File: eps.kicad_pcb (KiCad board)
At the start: 4 copper layers, 90 x 96 mm, 43 parts, among them J1 Barrel_Jack, U1 LT3652EMSE

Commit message: Solved errors
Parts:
- moved J1 12.0 mm to (118.7, 106.0)
- moved D9 3.71 mm to (169.0, 36.0)
- moved REF** 1.72 mm to (103.0, 126.0)
- moved REF** 1.47 mm to (103.0, 36.0)
- moved REF** 1.39 mm to (187.0, 126.0)
- moved D10 1.33 mm to (161.3, 36.1)
- moved REF** 1.06 mm to (187.0, 36.0)
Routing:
- net Net-(U1-SENSE): track 33.5 -> 19.9 mm
- net GND: track 275.2 -> 286.4 mm
- net Net-(D7-A): track 56.3 -> 61.5 mm
- net /BatteryCharger/in: track 100.4 -> 96.9 mm
- net Net-(D9-K): track 9.61 -> 8.70 mm
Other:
- outline, holes or cut-outs redrawn
- board text added: "Hydrogen v0.1"
- board text added: "Ulog3"

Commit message: final
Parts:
- added J2: Conn_01x02_Pin, Connector_PinHeader_2.00mm:PinHeader_1x02_P2.00mm_Vertical, B.Cu at (126.0, 34.0)
- SC1, SC2, SC3, SC4, SC5, SC6: footprint Connector_PinHeader_1.00mm:PinHeader_2x01_P1.00mm_Vertical -> Connector_PinHeader_2.00mm:PinHeader_1x02_P2.00mm_Vertical
- moved D9 7.51 mm to (176.3, 34.0)
- moved SC6 7.27 mm to (162.0, 34.0), turned to -90 degrees
- moved D10 6.76 mm to (167.8, 34.1)
- moved SC5 5.50 mm to (156.0, 34.0), turned to -90 degrees
- moved SC4 3.79 mm to (149.9, 34.0), turned to -90 degrees
- moved SC1 2.56 mm to (131.6, 34.0), turned to -90 degrees
- moved SC3 2.25 mm to (143.8, 34.0), turned to -90 degrees
- moved SC2 1.57 mm to (137.7, 34.0), turned to -90 degrees
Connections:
- net VBUS renamed /BatteryCharger/load
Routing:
- net /BatteryCharger/load: track 33.6 -> 61.0 mm
- net Net-(U1-SENSE): track 19.9 -> 46.2 mm
- net GND: track 286.4 -> 302.3 mm
- net /BatteryCharger/in: track 96.9 -> 110.8 mm
- net Net-(D9-K): track 8.70 -> 10.7 mm
- net Net-(D2-A): track 6.74 -> 8.53 mm
- net Net-(D3-A): track 6.81 -> 8.12 mm
- net Net-(D1-A): track 6.99 -> 8.11 mm
- net Net-(D4-A): track 7.36 -> 8.33 mm
- net Net-(D5-A): track 7.91 -> 8.54 mm
- net Net-(D10-K): track 9.74 -> 9.18 mm

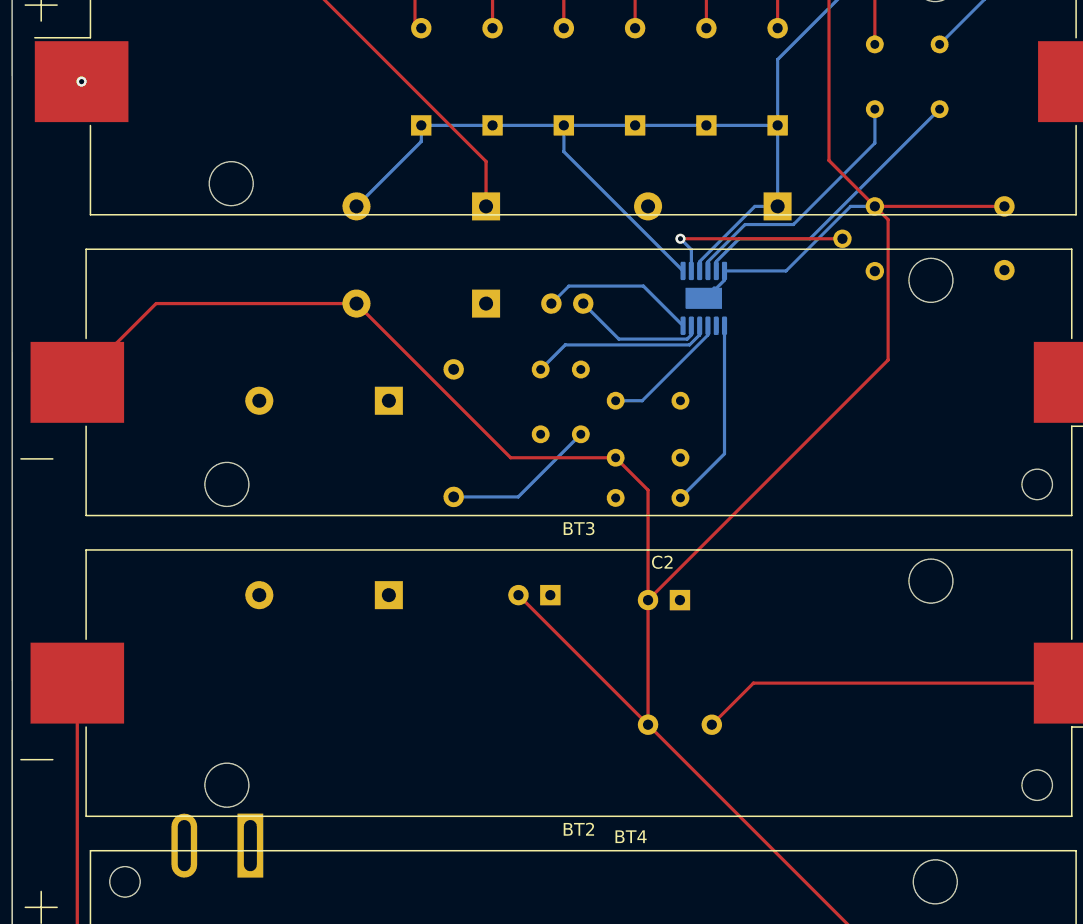
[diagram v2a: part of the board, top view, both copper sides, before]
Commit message: 2layerconversion
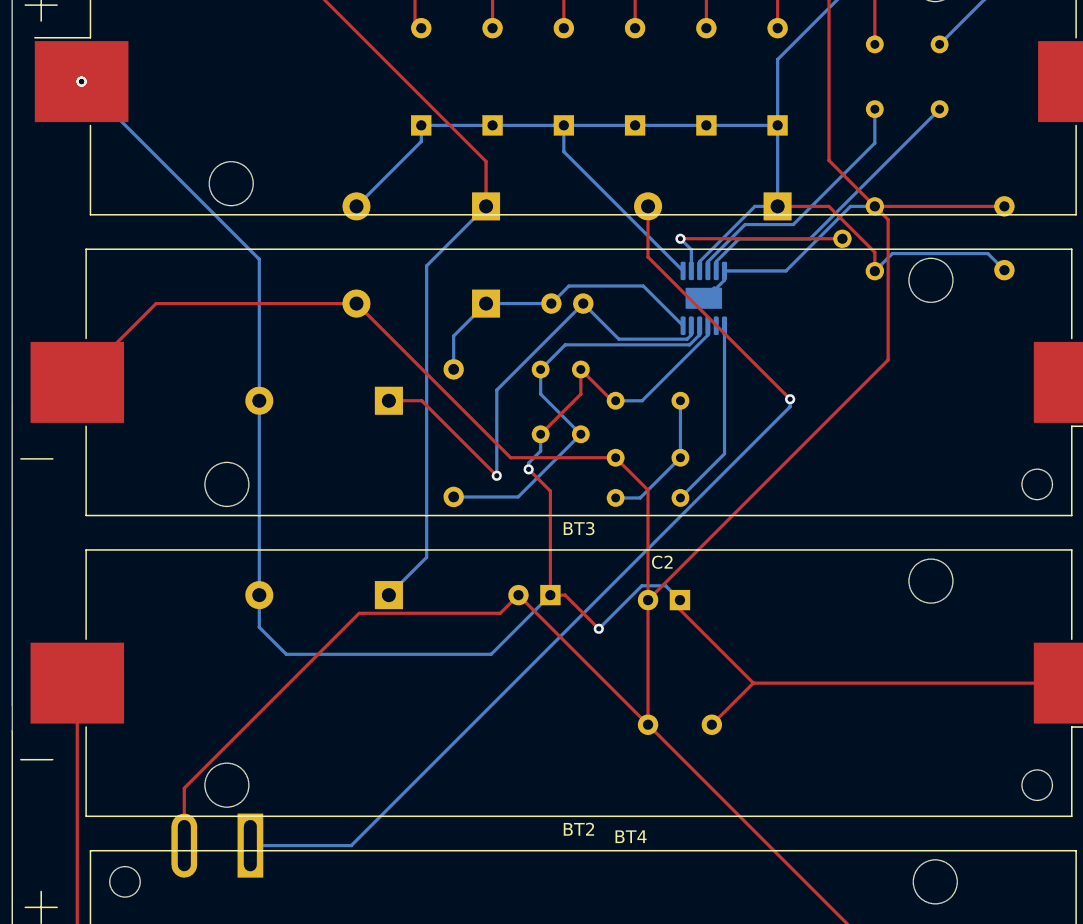
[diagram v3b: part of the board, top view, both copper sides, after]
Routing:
- net Net-(D7-A): track 61.5 -> 76.9 mm, vias 0 -> 1
- net Net-(U1-SENSE): track 46.2 -> 33.4 mm
- net Net-(D11-K): track 28.9 -> 37.7 mm, vias 0 -> 1
- net Net-(BT1-+): track 158.2 -> 163.0 mm, vias 1 -> 4
- net GND: track 302.3 -> 300.9 mm
- net /BatteryCharger/in: track 110.8 -> 111.7 mm
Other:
- copper layers 4 -> 2

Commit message: Added
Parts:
- added J3: Conn_01x02_Pin, Connector_PinHeader_2.00mm:PinHeader_1x02_P2.00mm_Vertical, B.Cu at (88.0, 43.9)
- added J4: Conn_01x02_Pin, Connector_PinHeader_2.00mm:PinHeader_1x02_P2.00mm_Vertical, B.Cu at (83.9, 43.9)
- added J5: Conn_01x02_Pin, Connector_PinHeader_2.00mm:PinHeader_1x02_P2.00mm_Vertical, B.Cu at (79.9, 43.9)
- added J6: Conn_01x02_Pin, Connector_PinHeader_2.00mm:PinHeader_1x02_P2.00mm_Vertical, B.Cu at (75.8, 43.9)
- added R8: R, Resistor_THT:R_Axial_DIN0204_L3.6mm_D1.6mm_P5.08mm_Horizontal, B.Cu at (88.5, 51.5)
- added R9: R, Resistor_THT:R_Axial_DIN0204_L3.6mm_D1.6mm_P5.08mm_Horizontal, B.Cu at (78.5, 51.5)
- added U2: INA234AxYBJ, Package_BGA:Texas_DSBGA-8_0.705x1.468mm_Layout2x4_P0.4mm, B.Cu at (88.1, 55.3)
- added U3: INA234AxYBJ, Package_BGA:Texas_DSBGA-8_0.705x1.468mm_Layout2x4_P0.4mm, B.Cu at (78.1, 55.3)
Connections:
- net /BatteryCharger/load renamed +5V
- D1 pad 1: /BatteryCharger/in -> /Power sensor/source
- D13 pad 2: Net-(BT1-+) -> Net-(D13-A)
- D2 pad 1: /BatteryCharger/in -> /Power sensor/source
- D3 pad 1: /BatteryCharger/in -> /Power sensor/source
- D4 pad 1: /BatteryCharger/in -> /Power sensor/source
- D5 pad 1: /BatteryCharger/in -> /Power sensor/source
- D6 pad 1: /BatteryCharger/in -> /Power sensor/source

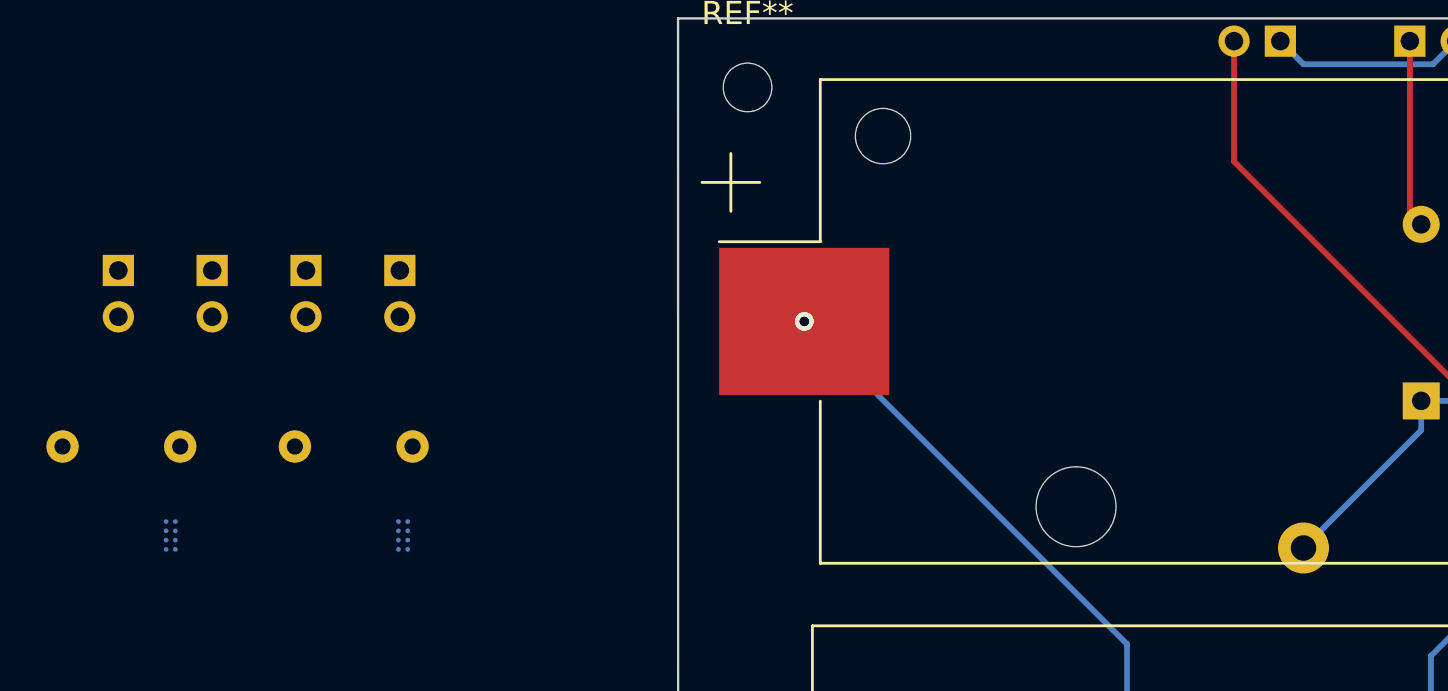
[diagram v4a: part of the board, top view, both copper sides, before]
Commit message: changed placement
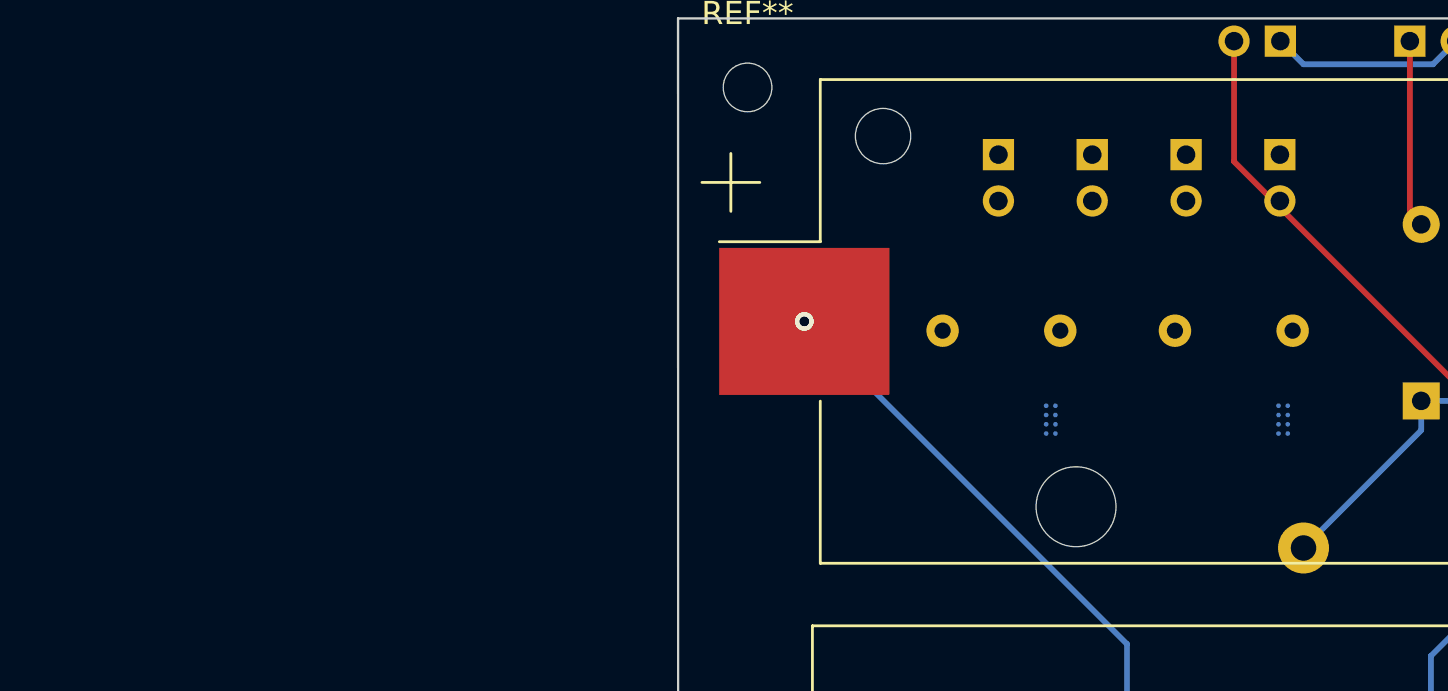
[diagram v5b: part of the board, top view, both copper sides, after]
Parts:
- moved J3 38.3 mm to (126.0, 38.9)
- moved J4 38.3 mm to (121.9, 38.9)
- moved U2 38.3 mm to (126.1, 50.3)
- moved U3 38.3 mm to (116.1, 50.3)
- moved J5 38.3 mm to (117.9, 38.9)
- moved J6 38.3 mm to (113.8, 38.9)
- moved R8 38.3 mm to (126.5, 46.5)
- moved R9 38.3 mm to (116.5, 46.5)
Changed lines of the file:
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@@
 	(footprint "Package_BGA:Texas_DSBGA-8_0.705x1.468mm_Layout2x4_P0.4mm"
 		(layer "B.Cu")
-		(at 88.13 55.34 180)
+		(at 126.12 50.34 180)
 		(descr "Texas Instruments, DSBGA, area grid, NSMD, YBJ0008 pad definition, 0.705x1.468mm, 8 Ball, 2x4 Layout, 0.4mm Pitch, https://www.ti.com/lit/gpn/ina234")
 		(tags "BGA 8 0.4")
@@
 	(footprint "Connector_PinHeader_2.00mm:PinHeader_1x02_P2.00mm_Vertical"
 		(layer "B.Cu")
-		(at 83.94 43.9 180)
+		(at 121.93 38.9 180)
 		(descr "Through hole straight pin header, 1x02, 2.00mm pitch, single row")
 		(tags "Through hole pin header THT 1x02 2.00mm single row")
@@
 	(footprint "Connector_PinHeader_2.00mm:PinHeader_1x02_P2.00mm_Vertical"
 		(layer "B.Cu")
-		(at 75.84 43.9 180)
+		(at 113.83 38.9 180)
 		(descr "Through hole straight pin header, 1x02, 2.00mm pitch, single row")
 		(tags "Through hole pin header THT 1x02 2.00mm single row")
@@
 	(footprint "Resistor_THT:R_Axial_DIN0204_L3.6mm_D1.6mm_P5.08mm_Horizontal"
 		(layer "B.Cu")
-		(at 78.51 51.5 180)
+		(at 116.5 46.5 180)
 		(descr "Resistor, Axial_DIN0204 series, Axial, Horizontal, pin pitch=5.08mm, 0.167W, length*diameter=3.6*1.6mm^2, http://cdn-reichelt.de/documents/datenblatt/B400/1_4W%23YAG.pdf")
 		(tags "Resistor Axial_DIN0204 series Axial Horizontal pin pitch 5.08mm 0.167W length 3.6mm diameter 1.6mm")
@@
 	(footprint "Connector_PinHeader_2.00mm:PinHeader_1x02_P2.00mm_Vertical"
 		(layer "B.Cu")
-		(at 87.99 43.9 180)
+		(at 125.98 38.9 180)
 		(descr "Through hole straight pin header, 1x02, 2.00mm pitch, single row")
 		(tags "Through hole pin header THT 1x02 2.00mm single row")
@@
 	(footprint "Resistor_THT:R_Axial_DIN0204_L3.6mm_D1.6mm_P5.08mm_Horizontal"
 		(layer "B.Cu")
-		(at 88.54 51.5 180)
+		(at 126.53 46.5 180)
 		(descr "Resistor, Axial_DIN0204 series, Axial, Horizontal, pin pitch=5.08mm, 0.167W, length*diameter=3.6*1.6mm^2, http://cdn-reichelt.de/documents/datenblatt/B400/1_4W%23YAG.pdf")
 		(tags "Resistor Axial_DIN0204 series Axial Horizontal pin pitch 5.08mm 0.167W length 3.6mm diameter 1.6mm")
@@
 	(footprint "Package_BGA:Texas_DSBGA-8_0.705x1.468mm_Layout2x4_P0.4mm"
 		(layer "B.Cu")
-		(at 78.1 55.34 180)
+		(at 116.09 50.34 180)
 		(descr "Texas Instruments, DSBGA, area grid, NSMD, YBJ0008 pad definition, 0.705x1.468mm, 8 Ball, 2x4 Layout, 0.4mm Pitch, https://www.ti.com/lit/gpn/ina234")
 		(tags "BGA 8 0.4")
@@
 	(footprint "Connector_PinHeader_2.00mm:PinHeader_1x02_P2.00mm_Vertical"
 		(layer "B.Cu")
-		(at 79.89 43.9 180)
+		(at 117.88 38.9 180)
 		(descr "Through hole straight pin header, 1x02, 2.00mm pitch, single row")
 		(tags "Through hole pin header THT 1x02 2.00mm single row")

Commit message: new design
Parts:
- removed BT3, BT4: Battery_Cell, Battery:BatteryHolder_Keystone_1042_1x18650
- removed D11, D12, D13: 1N5819, Diode_THT:D_DO-41_SOD81_P10.16mm_Horizontal
- removed J1: Barrel_Jack, Connector_BarrelJack:BarrelJack_SwitchcraftConxall_RAPC10U_Horizontal
- removed J4, J5, J6: Conn_01x02_Pin, Connector_PinHeader_2.00mm:PinHeader_1x02_P2.00mm_Vertical
- removed the REF** at (103.0, 126.0)
- removed the REF** at (187.0, 126.0)
- removed the REF** at (187.0, 36.0)
- removed the REF** at (103.0, 36.0)
- removed RV1: 10k, Potentiometer_THT:Potentiometer_Bourns_3386P_Vertical
- added C10: 10uF 16V, Capacitor_SMD:C_0805_2012Metric_Pad1.18x1.45mm_HandSolder, F.Cu at (95.9, 148.6)
- added C11: 1uF, Capacitor_SMD:C_0603_1608Metric_Pad1.08x0.95mm_HandSolder, F.Cu at (97.9, 148.6)
- added C6: 0.1uF 10V, Capacitor_SMD:C_0201_0603Metric_Pad0.64x0.40mm_HandSolder, F.Cu at (136.0, 92.5)
- added C7: 10uF 10V, Capacitor_SMD:C_0805_2012Metric_Pad1.18x1.45mm_HandSolder, F.Cu at (132.0, 92.5)
- added C8: 1uF 50V, Capacitor_SMD:C_0402_1005Metric_Pad0.74x0.62mm_HandSolder, F.Cu at (113.9, 154.0)
- added C9: 100uF 10V, Capacitor_THT:C_Radial_D5.0mm_H11.0mm_P2.00mm, F.Cu at (121.0, 149.0)
- added L2: 10uH, Inductor_SMD:L_2512_6332Metric_Pad1.52x3.35mm_HandSolder, F.Cu at (121.5, 156.0)
- added R10: 100k, Resistor_THT:R_Axial_DIN0207_L6.3mm_D2.5mm_P15.24mm_Horizontal, F.Cu at (91.6, 87.3)
- added R11: 0.068, Resistor_THT:R_Axial_DIN0207_L6.3mm_D2.5mm_P15.24mm_Horizontal, F.Cu at (115.1, 150.1)
- added R12: 430k, Resistor_THT:R_Axial_DIN0207_L6.3mm_D2.5mm_P15.24mm_Horizontal, F.Cu at (78.3, 146.6)
- added R13: 606k, Resistor_THT:R_Axial_DIN0207_L6.3mm_D2.5mm_P15.24mm_Horizontal, F.Cu at (78.3, 150.1)
- added R14: 0.1, Resistor_THT:R_Axial_DIN0207_L6.3mm_D2.5mm_P15.24mm_Horizontal, F.Cu at (115.1, 146.6)
- added REF**: MountingHole_5mm, MountingHole:MountingHole_5mm, F.Cu at (132.0, 152.0)
- added REF**: MountingHole_5mm, MountingHole:MountingHole_5mm, F.Cu at (58.0, 152.0)
- added REF**: MountingHole_5mm, MountingHole:MountingHole_5mm, F.Cu at (132.5, 72.0)
- added REF**: MountingHole_5mm, MountingHole:MountingHole_5mm, F.Cu at (57.5, 72.0)
- BT1, BT2: value Battery_Cell -> 3.7v
- C1: value 10uF -> 2.2uF; footprint Capacitor_THT:C_Disc_D5.1mm_W3.2mm_P5.00mm -> Capacitor_SMD:C_0402_1005Metric_Pad0.74x0.62mm_HandSolder; moved to F.Cu
- C2: value 100uF -> 0.1uF; footprint Capacitor_THT:CP_Radial_D6.3mm_P2.50mm -> Capacitor_SMD:C_0603_1608Metric_Pad1.08x0.95mm_HandSolder; moved to F.Cu
- C3: value 1uF -> 10nF; footprint Capacitor_THT:C_Disc_D5.0mm_W2.5mm_P2.50mm -> Capacitor_SMD:C_0805_2012Metric_Pad1.18x1.45mm_HandSolder; moved to F.Cu
- C4: value 10uF -> 100pF; footprint Capacitor_THT:C_Disc_D5.1mm_W3.2mm_P5.00mm -> Capacitor_SMD:C_0402_1005Metric_Pad0.74x0.62mm_HandSolder; moved to F.Cu
- C5: value 100uF 16v -> 470pF; footprint Capacitor_THT:CP_Radial_D6.3mm_P2.50mm -> Capacitor_SMD:C_0603_1608Metric_Pad1.08x0.95mm_HandSolder; moved to F.Cu
- D1, D2, D3, D4, D5, D6: moved to F.Cu
- D10, D9: footprint LED_THT:LED_Rectangular_W3.0mm_H2.0mm -> LED_THT:LED_D5.0mm; moved to F.Cu
- D7: value 1N5819 -> MBR340; footprint Diode_THT:D_DO-41_SOD81_P10.16mm_Horizontal -> Diode_THT:D_DO-201AD_P15.24mm_Horizontal; moved to F.Cu
- D8: value 1N5819 -> 1N5817; moved to F.Cu
- J2: value Conn_01x02_Pin -> Out-; footprint Connector_PinHeader_2.00mm:PinHeader_1x02_P2.00mm_Vertical -> Connector_PinHeader_2.54mm:PinHeader_1x02_P2.54mm_Vertical; moved to F.Cu
- J3: value Conn_01x02_Pin -> NTC_PIN; footprint Connector_PinHeader_2.00mm:PinHeader_1x02_P2.00mm_Vertical -> Connector_PinHeader_2.54mm:PinHeader_1x02_P2.54mm_Vertical; moved to F.Cu
- L1: value 68uH -> 4.7uH; footprint Inductor_THT:L_Axial_L5.0mm_D3.6mm_P10.00mm_Horizontal_Murata_BL01RN1A2A2 -> Inductor_THT:L_Radial_D8.7mm_P5.00mm_Fastron_07HCP; moved to F.Cu
- R1: value 568k -> 17.8k; footprint Resistor_THT:R_Axial_DIN0204_L3.6mm_D1.6mm_P5.08mm_Horizontal -> Resistor_THT:R_Axial_DIN0207_L6.3mm_D2.5mm_P15.24mm_Horizontal; moved to F.Cu
- R2, R3: footprint Resistor_THT:R_Axial_DIN0204_L3.6mm_D1.6mm_P5.08mm_Horizontal -> Resistor_THT:R_Axial_DIN0207_L6.3mm_D2.5mm_P15.24mm_Horizontal; moved to F.Cu
- R4: value 0.22 -> 4.32k; footprint Resistor_THT:R_Axial_DIN0204_L3.6mm_D1.6mm_P5.08mm_Horizontal -> Resistor_THT:R_Axial_DIN0207_L6.3mm_D2.5mm_P15.24mm_Horizontal; moved to F.Cu
- R5: value 0.5 -> 200k; footprint Resistor_THT:R_Axial_DIN0204_L3.6mm_D1.6mm_P5.08mm_Horizontal -> Resistor_THT:R_Axial_DIN0207_L6.3mm_D2.5mm_P15.24mm_Horizontal; moved to F.Cu
- R6: value 446k -> 23.2k; footprint Resistor_THT:R_Axial_DIN0204_L3.6mm_D1.6mm_P5.08mm_Horizontal -> Resistor_THT:R_Axial_DIN0207_L6.3mm_D2.5mm_P15.24mm_Horizontal; moved to F.Cu
- R7: value 200k -> 38.3k; footprint Resistor_THT:R_Axial_DIN0204_L3.6mm_D1.6mm_P5.08mm_Horizontal -> Resistor_THT:R_Axial_DIN0207_L6.3mm_D2.5mm_P15.24mm_Horizontal; moved to F.Cu
- R8: value R -> 100k; footprint Resistor_THT:R_Axial_DIN0204_L3.6mm_D1.6mm_P5.08mm_Horizontal -> Resistor_THT:R_Axial_DIN0207_L6.3mm_D2.5mm_P15.24mm_Horizontal; moved to F.Cu
- R9: value R -> 210k; footprint Resistor_THT:R_Axial_DIN0204_L3.6mm_D1.6mm_P5.08mm_Horizontal -> Resistor_THT:R_Axial_DIN0207_L6.3mm_D2.5mm_P15.24mm_Horizontal; moved to F.Cu
- SC1, SC2, SC3, SC4, SC5, SC6: footprint Connector_PinHeader_2.00mm:PinHeader_1x02_P2.00mm_Vertical -> Connector_PinHeader_2.54mm:PinHeader_1x02_P2.54mm_Vertical; moved to F.Cu
- U1: value LT3652EMSE -> LT3652IMSE; moved to F.Cu
- U2: value INA234AxYBJ -> CMSH3-40MA; footprint Package_BGA:Texas_DSBGA-8_0.705x1.468mm_Layout2x4_P0.4mm -> CMSH3-40MA:SMA; moved to F.Cu
- U3: value INA234AxYBJ -> LT3479EDE_TRPBF; footprint Package_BGA:Texas_DSBGA-8_0.705x1.468mm_Layout2x4_P0.4mm -> LT3479EDE_TRPBF:DFN-14_DE; moved to F.Cu
- moved R2 141.4 mm to (78.3, 153.5), turned to 0 degrees
- moved R3 141.2 mm to (78.3, 157.6), turned to 0 degrees
- moved D9 131.7 mm to (54.5, 84.0), turned to 0 degrees
- moved D10 128.0 mm to (54.5, 93.5)
- moved U1 126.5 mm to (68.6, 156.2), turned to 0 degrees
- moved J3 122.1 mm to (69.4, 147.1), turned to -90 degrees
- moved U2 116.1 mm to (68.4, 151.0)
- moved J2 114.0 mm to (53.5, 122.0), turned to 180 degrees
- moved BT1 99.7 mm to (96.0, 133.0), turned to 180 degrees
- moved SC6 97.7 mm to (71.2, 69.9), turned to 180 degrees
- moved D6 94.9 mm to (71.0, 82.3)
- moved D8 93.9 mm to (110.4, 153.6)
- moved SC5 88.0 mm to (75.7, 69.9), turned to 180 degrees
- moved D5 85.5 mm to (75.5, 82.3)
- moved C1 84.5 mm to (96.5, 84.0), turned to 0 degrees
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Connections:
- BT1 pad 2: Net-(BT1--) -> GND
- BT2 pad 1: Net-(BT1-+) -> +5V
- BT2 pad 2: Net-(BT2--) -> Net-(BT1-+)
- C2 pad 1: Net-(BT1-+) -> Net-(U3-SS)
- C3 pad 1: Net-(D11-K) -> Net-(C3-Pad1)
- C3 pad 2: Net-(D8-K) -> GND
- C4 pad 1: Net-(BT1-+) -> Net-(U3-FBP)
- C5 pad 1: Net-(BT1-+) -> Net-(D7-K)
- C5 pad 2: GND -> Net-(U3-FBN)
- D1 pad 1: /Power sensor/source -> /BatteryCharger/in
- D2 pad 1: /Power sensor/source -> /BatteryCharger/in
- D3 pad 1: /Power sensor/source -> /BatteryCharger/in
- D4 pad 1: /Power sensor/source -> /BatteryCharger/in
- D5 pad 1: /Power sensor/source -> /BatteryCharger/in
- D6 pad 1: /Power sensor/source -> /BatteryCharger/in
- D7 pad 1: /BatteryCharger/in -> Net-(D7-K)
- D8 pad 2: GND -> +5V
- J3 pad 1: /Power sensor/scl -> Net-(J3-Pin_1)
- J3 pad 2: /Power sensor/sda -> GND
- L1 pad 1: Net-(D8-K) -> Net-(U3-L)
- L1 pad 2: Net-(U1-SENSE) -> Net-(D7-A)
- R1 pad 1: Net-(BT1-+) -> Net-(U3-RT)
- R1 pad 2: Net-(R1-Pad2) -> GND
- R4 pad 1: Net-(U1-SENSE) -> Net-(U3-VC)
- R4 pad 2: Net-(BT1-+) -> Net-(C3-Pad1)
- R5 pad 1: Net-(BT1-+) -> Net-(D7-K)
- R5 pad 2: Net-(U1-SENSE) -> Net-(U3-FBN)
- R6 pad 1: Net-(R1-Pad2) -> Net-(U3-FBN)
- R7 pad 1: Net-(U1-V_{FB}) -> /BatteryCharger/in
- R7 pad 2: Net-(R1-Pad2) -> Net-(U1-V_{IN_REG})
- R8 pad 1: Net-(D13-A) -> Net-(U1-V_{IN_REG})
- R8 pad 2: Net-(BT1-+) -> GND
- R9 pad 1: /Power sensor/source -> /BatteryCharger/in
- R9 pad 2: /BatteryCharger/in -> Net-(U1-~{SHDN})
- U1 pad 1: /BatteryCharger/in -> Net-(D7-K)
- U1 pad 11: Net-(D11-K) -> Net-(D8-K)
- U1 pad 12: Net-(D8-K) -> Net-(U1-SW)
- U1 pad 3: /BatteryCharger/in -> Net-(U1-~{SHDN})
- U1 pad 8: unconnected-(U1-NTC-Pad8) -> Net-(J3-Pin_1)
- U1 pad 9: Net-(BT1-+) -> +5V
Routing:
- net Net-(BT1-+): track 163.0 -> 24.0 mm, vias 4 -> 0
- net Net-(D7-K): track 0.00 -> 136.6 mm, vias 0 -> 1
- net Net-(D10-K): track 9.18 -> 142.0 mm, vias 0 -> 1
- net Net-(D9-K): track 10.7 -> 133.8 mm, vias 0 -> 1
- net Net-(U1-~{SHDN}): track 0.00 -> 84.1 mm
- net +5V: track 61.0 -> 136.5 mm
- net Net-(U1-V_{IN_REG}): track 15.6 -> 79.6 mm, vias 1 -> 0
- net Net-(U1-SW): track 0.00 -> 61.0 mm, vias 0 -> 2
- net GND: track 300.9 -> 359.4 mm
- net Net-(U3-FBN): track 0.00 -> 54.7 mm, vias 0 -> 4
- net Net-(D7-A): track 76.9 -> 25.9 mm, vias 1 -> 0
- net Net-(D11-K): track 37.7 -> 0.00 mm, vias 1 -> 0
- net Net-(U3-L): track 0.00 -> 33.2 mm
- net Net-(U3-VC): track 0.00 -> 31.7 mm, vias 0 -> 1
- net Net-(J3-Pin_1): track 0.00 -> 29.7 mm, vias 0 -> 1
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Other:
- outline, holes or cut-outs redrawn
- board text removed: "Hydrogen v0.1"
- board text removed: "Ulog3"

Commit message: fixed
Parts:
- J2: value Out- -> Conn_01x02_Pin
- U3: footprint LT3479EDE_TRPBF:DFN-14_DE -> footprints:DFN-14_DE_LIT-L
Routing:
- net /BatteryCharger/in: track 82.7 -> 91.3 mm
- net Net-(U3-VC): track 31.7 -> 29.7 mm
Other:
- board text added: "Helium v0.2"
